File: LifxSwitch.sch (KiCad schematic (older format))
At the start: 3 parts

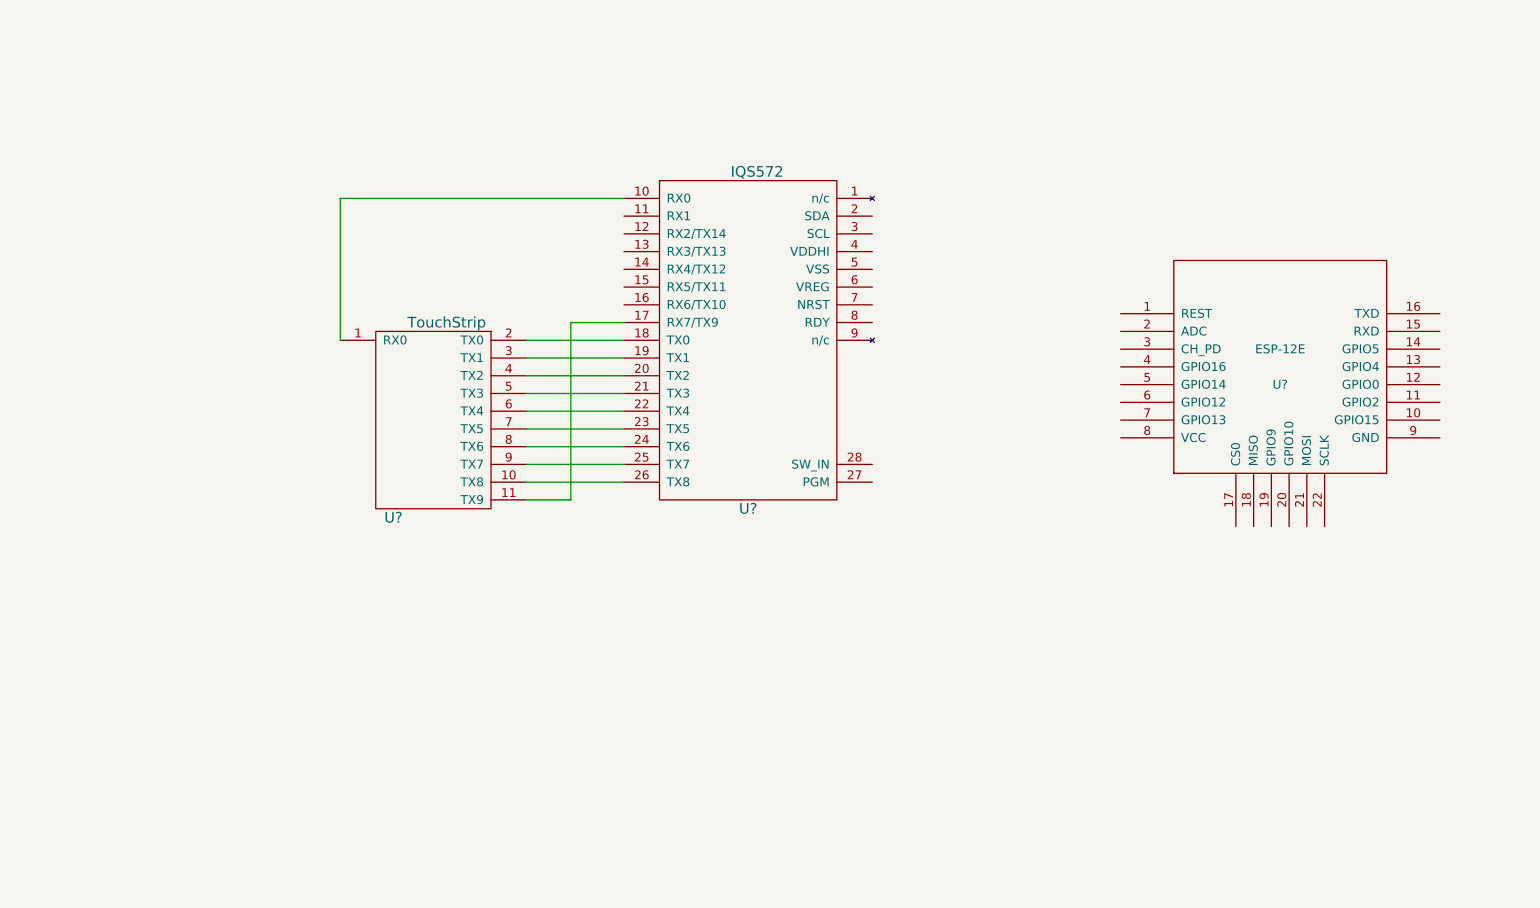
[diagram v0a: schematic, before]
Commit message: Added some wires and pads
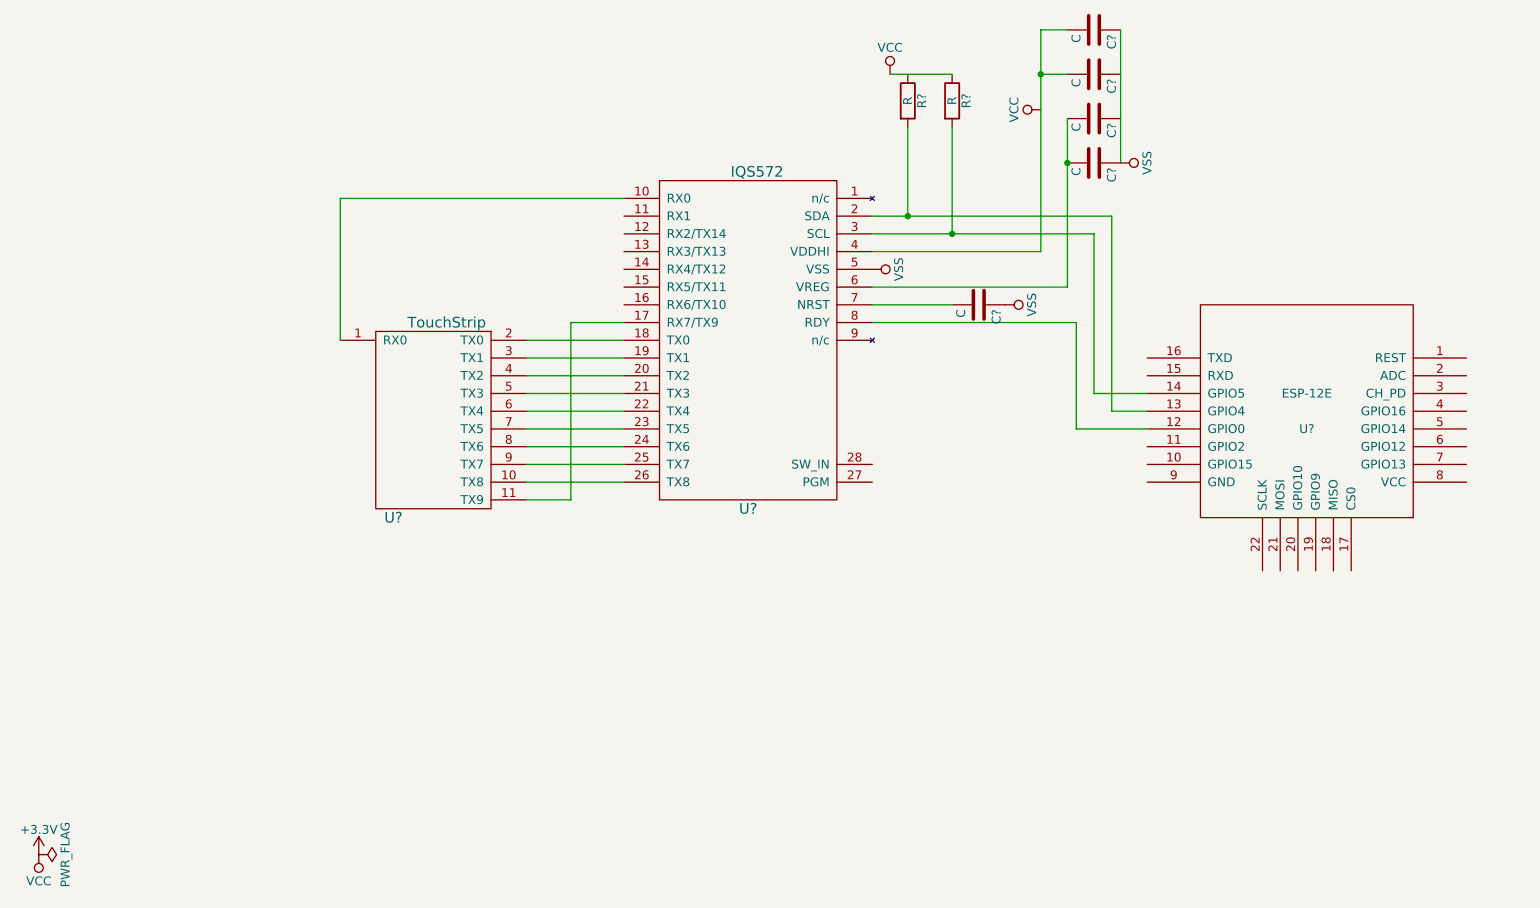
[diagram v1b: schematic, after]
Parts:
- added C? (x5): C, symbol C
- added R? (x2): R, symbol R
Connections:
- net at U?.2 (SDA): now also U?.13 (GPIO4), R?.2
- net at U?.3 (SCL): now also U?.14 (GPIO5), R?.2
- net at U?.4 (VDDHI): now also C?.2, C?.2
- net VSS: now reaches U?.5 (VSS)
- net VSS: now also C?.1, C?.1, C?.1
- net at U?.6 (VREG): now also C?.2, C?.2
- net at U?.7 (NRST): now also C?.2
- net at U?.8 (RDY): now also U?.12 (GPIO0)
- new net +3V3: R?.1
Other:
- moved on the sheet: U?
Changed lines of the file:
@@
-$EndComp
-$Comp
-L ESP-12E U?
-U 1 1 5B29B2F9
-P 9050 3350
-F 0 "U?" H 9050 3250 50  0000 C CNN
-F 1 "ESP-12E" H 9050 3450 50  0000 C CNN
-F 2 "" H 9050 3350 50  0001 C CNN
-F 3 "" H 9050 3350 50  0001 C CNN
-	1    9050 3350
-	1    0    0    -1
 $EndComp
 $Comp
@@
 Wire Wire Line
 	5050 3100 5350 3100
+$Comp
+L +3.3V #PWR?
+U 1 1 5B29D947
+P 2050 6100
+F 0 "#PWR?" H 2050 5950 50  0001 C CNN
+F 1 "+3.3V" H 2050 6240 50  0000 C CNN
+F 2 "" H 2050 6100 50  0001 C CNN
+F 3 "" H 2050 6100 50  0001 C CNN
+	1    2050 6100
+	1    0    0    -1
+$EndComp
+$Comp
+L VCC #PWR?
+U 1 1 5B29D961
+P 2050 6100
+F 0 "#PWR?" H 2050 5950 50  0001 C CNN
+F 1 "VCC" H 2050 6250 50  0000 C CNN
+F 2 "" H 2050 6100 50  0001 C CNN
+F 3 "" H 2050 6100 50  0001 C CNN
+	1    2050 6100
+	-1   0    0    1
+$EndComp
+$Comp
+L PWR_FLAG #FLG?
+U 1 1 5B29D97B
+P 2050 6100
+F 0 "#FLG?" H 2050 6175 50  0001 C CNN
+F 1 "PWR_FLAG" H 2050 6250 50  0000 C CNN
+F 2 "" H 2050 6100 50  0001 C CNN
+F 3 "" H 2050 6100 50  0001 C CNN
+	1    2050 6100
+	0    1    1    0
+$EndComp
+Wire Wire Line
+	7700 2700 6750 2700
+Wire Wire Line
+	7700 1450 7700 2700
+$Comp
+L VCC #PWR?
+U 1 1 5B29D9E3
+P 7700 1900
+F 0 "#PWR?" H 7700 1750 50  0001 C CNN
+F 1 "VCC" H 7700 2050 50  0000 C CNN
+F 2 "" H 7700 1900 50  0001 C CNN
+F 3 "" H 7700 1900 50  0001 C CNN
+	1    7700 1900
+	0    -1   -1   0
+$EndComp
+Wire Wire Line
+	7700 1450 7850 1450
+$Comp
+L C C?
+U 1 1 5B29DA14
+P 8000 1450
+F 0 "C?" H 8025 1550 50  0000 L CNN
+F 1 "C" H 8025 1350 50  0000 L CNN
+F 2 "" H 8038 1300 50  0001 C CNN
+F 3 "" H 8000 1450 50  0001 C CNN
+	1    8000 1450
+	0    1    1    0
+$EndComp
+$Comp
+L C C?
+U 1 1 5B29DA41
+P 8000 1700
+F 0 "C?" H 8025 1800 50  0000 L CNN
+F 1 "C" H 8025 1600 50  0000 L CNN
+F 2 "" H 8038 1550 50  0001 C CNN
+F 3 "" H 8000 1700 50  0001 C CNN
+	1    8000 1700
+	0    1    1    0
+$EndComp
+Wire Wire Line
+	7700 1700 7850 1700
+Connection ~ 7700 1700
+Wire Wire Line
+	7850 2900 6750 2900
+Wire Wire Line
+	7850 1950 7850 2900
+$Comp
+L C C?
+U 1 1 5B29DA9C
+P 8000 2200
+F 0 "C?" H 8025 2300 50  0000 L CNN
+F 1 "C" H 8025 2100 50  0000 L CNN
+F 2 "" H 8038 2050 50  0001 C CNN
+F 3 "" H 8000 2200 50  0001 C CNN
+	1    8000 2200
+	0    1    1    0
+$EndComp
+Connection ~ 7850 2200
+$Comp
+L C C?
+U 1 1 5B29DAE8
+P 8000 1950
+F 0 "C?" H 8025 2050 50  0000 L CNN
+F 1 "C" H 8025 1850 50  0000 L CNN
+F 2 "" H 8038 1800 50  0001 C CNN
+F 3 "" H 8000 1950 50  0001 C CNN
+	1    8000 1950
+	0    1    1    0
+$EndComp
+Wire Wire Line
+	8150 2200 8150 1450
+$Comp
+L VSS #PWR?
+U 1 1 5B29DB55
+P 8150 2200
+F 0 "#PWR?" H 8150 2050 50  0001 C CNN
+F 1 "VSS" H 8150 2350 50  0000 C CNN
+F 2 "" H 8150 2200 50  0001 C CNN
+F 3 "" H 8150 2200 50  0001 C CNN
+	1    8150 2200
+	0    1    1    0
+$EndComp
+$Comp
+L C C?
+U 1 1 5B29DB98
+P 7350 3000
+F 0 "C?" H 7375 3100 50  0000 L CNN
+F 1 "C" H 7375 2900 50  0000 L CNN
+F 2 "" H 7388 2850 50  0001 C CNN
+F 3 "" H 7350 3000 50  0001 C CNN
+	1    7350 3000
+	0    1    1    0
+$EndComp
+Wire Wire Line
+	6750 3000 7200 3000
+$Comp
+L VSS #PWR?
+U 1 1 5B29DC08
+P 7500 3000
+F 0 "#PWR?" H 7500 2850 50  0001 C CNN
+F 1 "VSS" H 7500 3150 50  0000 C CNN
+F 2 "" H 7500 3000 50  0001 C CNN
+F 3 "" H 7500 3000 50  0001 C CNN
+	1    7500 3000
+	0    1    1    0
+$EndComp
+Wire Wire Line
+	6750 2600 8000 2600
+Wire Wire Line
+	7200 2600 7200 2000
+$Comp
+L R R?
+U 1 1 5B29DD46
+P 7200 1850
+F 0 "R?" V 7280 1850 50  0000 C CNN
+F 1 "R" V 7200 1850 50  0000 C CNN
+F 2 "" V 7130 1850 50  0001 C CNN
+F 3 "" H 7200 1850 50  0001 C CNN
+	1    7200 1850
+	1    0    0    -1
+$EndComp
+Wire Wire Line
+	6750 2500 8100 2500
+Wire Wire Line
+	6950 2500 6950 2000
+$Comp
+L R R?
+U 1 1 5B29DDDB
+P 6950 1850
+F 0 "R?" V 7030 1850 50  0000 C CNN
+F 1 "R" V 6950 1850 50  0000 C CNN
+F 2 "" V 6880 1850 50  0001 C CNN
+F 3 "" H 6950 1850 50  0001 C CNN
+	1    6950 1850
+	1    0    0    -1
+$EndComp
+Wire Wire Line
+	7200 1700 6850 1700
+$Comp
+L VCC #PWR?
+U 1 1 5B29DE59
+P 6850 1700
+F 0 "#PWR?" H 6850 1550 50  0001 C CNN
+F 1 "VCC" H 6850 1850 50  0000 C CNN
+F 2 "" H 6850 1700 50  0001 C CNN
+F 3 "" H 6850 1700 50  0001 C CNN
+	1    6850 1700
+	1    0    0    -1
+$EndComp
+$Comp
+L ESP-12E U?
+U 1 1 5B29B2F9
+P 9200 3600
+F 0 "U?" H 9200 3500 50  0000 C CNN
+F 1 "ESP-12E" H 9200 3700 50  0000 C CNN
+F 2 "" H 9200 3600 50  0001 C CNN
+F 3 "" H 9200 3600 50  0001 C CNN
+	1    9200 3600
+	-1   0    0    -1
+$EndComp
+Wire Wire Line
+	8100 2500 8100 3600
+Wire Wire Line
+	8100 3600 8300 3600
+Connection ~ 6950 2500
+Wire Wire Line
+	8000 2600 8000 3500
+Wire Wire Line
+	8000 3500 8300 3500
+Connection ~ 7200 2600
+$Comp
+L VSS #PWR?
+U 1 1 5B29DFC6
+P 6750 2800
+F 0 "#PWR?" H 6750 2650 50  0001 C CNN
+F 1 "VSS" H 6750 2950 50  0000 C CNN
+F 2 "" H 6750 2800 50  0001 C CNN
+F 3 "" H 6750 2800 50  0001 C CNN
+	1    6750 2800
+	0    1    1    0
+$EndComp
+Wire Wire Line
+	6750 3100 7900 3100
+Wire Wire Line
+	7900 3100 7900 3700
+Wire Wire Line
+	7900 3700 8300 3700
 $EndSCHEMATC

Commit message: Put some values in so I dont have to look them up later
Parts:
- C? (x2): value C -> 1uF
- C? (x2): value C -> 100pF
- C?: value C -> 100nF
- R? (x2): value R -> 4.7k
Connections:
- net +3V3: now also U?.8 (VCC)
- net VSS: now also U?.9 (GND)
- net LightStatus: now reaches U?.20 (GPIO10)
- net 100: now reaches U?.4 (GPIO16)
- net 75: now reaches U?.5 (GPIO14)
- net 50: now reaches U?.6 (GPIO12)
- net 25: now reaches U?.7 (GPIO13)
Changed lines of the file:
@@
 P 8000 1450
 F 0 "C?" H 8025 1550 50  0000 L CNN
-F 1 "C" H 8025 1350 50  0000 L CNN
+F 1 "1uF" H 8025 1350 50  0000 L CNN
 F 2 "" H 8038 1300 50  0001 C CNN
 F 3 "" H 8000 1450 50  0001 C CNN
@@
 P 8000 1700
 F 0 "C?" H 8025 1800 50  0000 L CNN
-F 1 "C" H 8025 1600 50  0000 L CNN
+F 1 "100pF" H 8025 1600 50  0000 L CNN
 F 2 "" H 8038 1550 50  0001 C CNN
 F 3 "" H 8000 1700 50  0001 C CNN
@@
 P 8000 2200
 F 0 "C?" H 8025 2300 50  0000 L CNN
-F 1 "C" H 8025 2100 50  0000 L CNN
+F 1 "100pF" H 8025 2100 50  0000 L CNN
 F 2 "" H 8038 2050 50  0001 C CNN
 F 3 "" H 8000 2200 50  0001 C CNN
@@
 P 8000 1950
 F 0 "C?" H 8025 2050 50  0000 L CNN
-F 1 "C" H 8025 1850 50  0000 L CNN
+F 1 "1uF" H 8025 1850 50  0000 L CNN
 F 2 "" H 8038 1800 50  0001 C CNN
 F 3 "" H 8000 1950 50  0001 C CNN
@@
 P 7350 3000
 F 0 "C?" H 7375 3100 50  0000 L CNN
-F 1 "C" H 7375 2900 50  0000 L CNN
+F 1 "100nF" H 7375 2900 50  0000 L CNN
 F 2 "" H 7388 2850 50  0001 C CNN
 F 3 "" H 7350 3000 50  0001 C CNN
@@
 P 7200 1850
 F 0 "R?" V 7280 1850 50  0000 C CNN
-F 1 "R" V 7200 1850 50  0000 C CNN
+F 1 "4.7k" V 7200 1850 50  0000 C CNN
 F 2 "" V 7130 1850 50  0001 C CNN
 F 3 "" H 7200 1850 50  0001 C CNN
@@
 P 6950 1850
 F 0 "R?" V 7030 1850 50  0000 C CNN
-F 1 "R" V 6950 1850 50  0000 C CNN
+F 1 "4.7k" V 6950 1850 50  0000 C CNN
 F 2 "" V 6880 1850 50  0001 C CNN
 F 3 "" H 6950 1850 50  0001 C CNN
@@
 Wire Wire Line
 	7900 3700 8300 3700
+Text GLabel 9150 4500 3    60   Input ~ 0
+LightStatus
+Text GLabel 10100 3900 2    60   Input ~ 0
+25
+Text GLabel 10100 3800 2    60   Input ~ 0
+50
+Text GLabel 10100 3700 2    60   Input ~ 0
+75
+Text GLabel 10100 3600 2    60   Input ~ 0
+100
+$Comp
+L VCC #PWR?
+U 1 1 5B29EAF7
+P 10100 4000
+F 0 "#PWR?" H 10100 3850 50  0001 C CNN
+F 1 "VCC" H 10100 4150 50  0000 C CNN
+F 2 "" H 10100 4000 50  0001 C CNN
+F 3 "" H 10100 4000 50  0001 C CNN
+	1    10100 4000
+	0    1    1    0
+$EndComp
+$Comp
+L VSS #PWR?
+U 1 1 5B29EB1F
+P 8300 4000
+F 0 "#PWR?" H 8300 3850 50  0001 C CNN
+F 1 "VSS" H 8300 4150 50  0000 C CNN
+F 2 "" H 8300 4000 50  0001 C CNN
+F 3 "" H 8300 4000 50  0001 C CNN
+	1    8300 4000
+	0    -1   -1   0
+$EndComp
 $EndSCHEMATC
